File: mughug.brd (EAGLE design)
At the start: 68.2 x 17.8 mm, 9 parts, among them J1 NEOPIXEL, U1 DS18B20

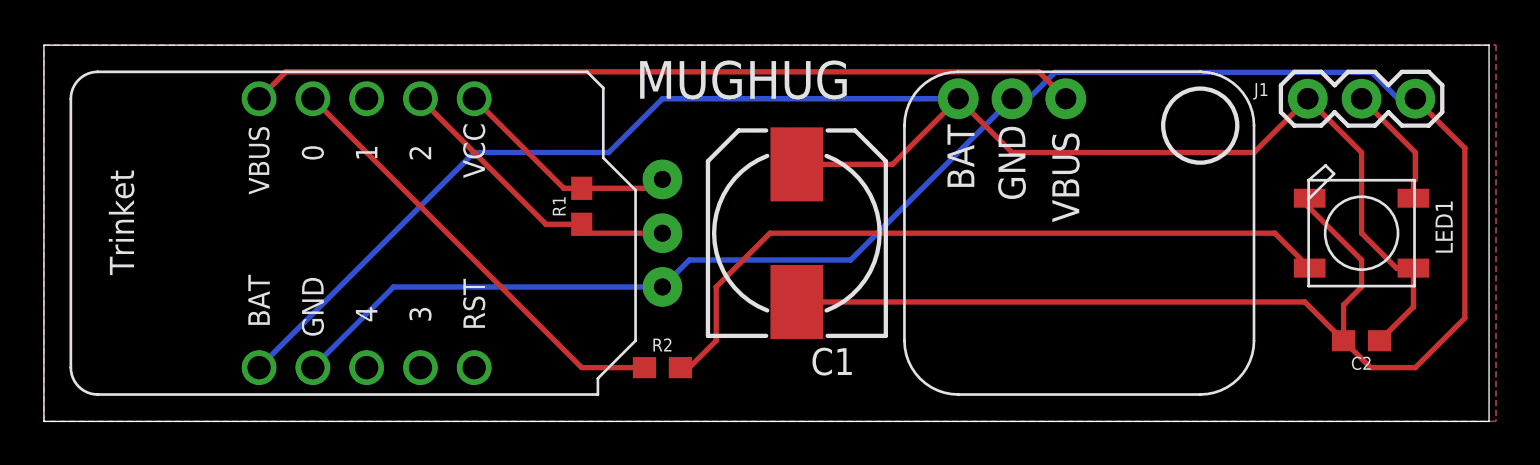
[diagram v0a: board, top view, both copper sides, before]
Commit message: Board reshuffle for oshpark
Added thicker board outline
moved neopixel to board center
small passived aligned same direction
12mil track for VBAT
added silkscreen
added corner holes for attachment
crossed fingers
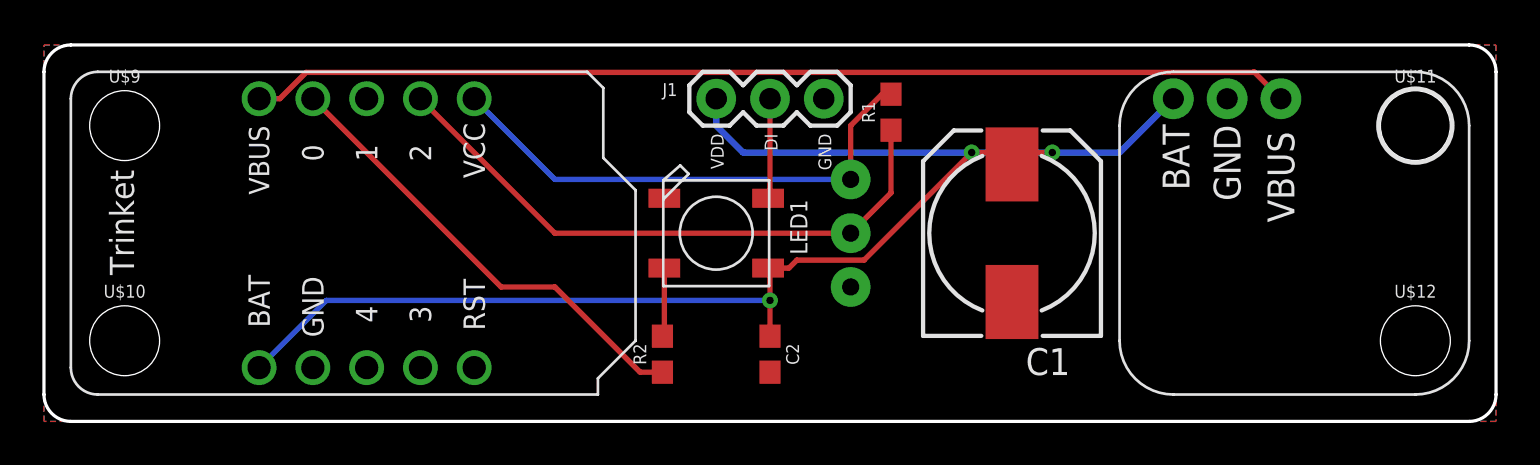
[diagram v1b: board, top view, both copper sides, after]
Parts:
- added U$10, U$11, U$12, U$9: (no value), SparkFun-Hardware:STAND-OFF
- moved LED1 30.5 mm to (31.8, 8.89)
- moved C2 27.9 mm to (34.3, 3.17), turned to 270 degrees
- moved J1 27.9 mm to (31.8, 15.2)
- moved R1 15.3 mm to (40.0, 14.6)
- moved U$2 10.2 mm to (58.4, 8.89)
- moved C1 10.2 mm to (45.7, 8.89)
- moved U1 8.89 mm to (38.1, 8.89)
- moved R2 0.63 mm to (29.2, 3.17), turned to 90 degrees
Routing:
- net GND: track 111.7 -> 0.00 mm
- net N$1: track 34.5 -> 3.25 mm
- net D2: track 14.1 -> 28.6 mm
- net VCC: track 10.8 -> 24.4 mm
- net VBAT: track 80.4 -> 69.2 mm, vias 0 -> 3
- net VBUS: track 39.2 -> 49.3 mm
- net N$4: track 5.79 -> 4.74 mm
- net D0: track 20.9 -> 21.9 mm
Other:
- board size 68.2 x 17.8 mm -> 68.6 x 17.8 mm
- board text added: "DI"
- board text added: "GND"
- board text added: "Troop 30226 TECHNOMANCERS"
- board text added: "VDD"

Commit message: Final tweak for oshpark proto order
oshpark order dm4ze97u
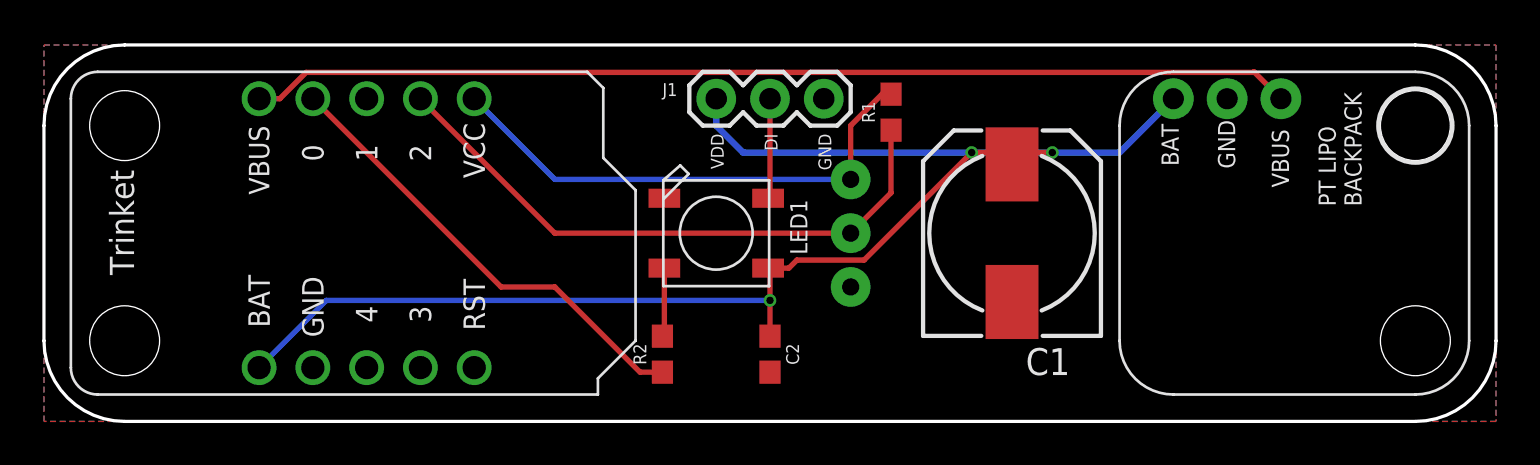
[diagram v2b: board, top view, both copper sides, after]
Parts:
- U$10, U$11, U$12, U$9: device SparkFun-Hardware:STAND-OFF -> redhunter:STAND-OFF
- U$2: value PROTRINKETLIPONOHOLE -> PROTRINKETLIPO
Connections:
- net VBUS: now also U$2.5V; no longer U$2.VBUS
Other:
- outline, holes or cut-outs redrawn
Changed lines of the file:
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@@
 <board>
 <plain>
-<wire x1="1.27" y1="0" x2="67.31" y2="0" width="0.1524" layer="20"/>
 <text x="54.61" y="3.81" size="1.778" layer="22" rot="MR0">MUGHUG</text>
-<wire x1="0" y1="16.51" x2="0" y2="1.27" width="0.1524" layer="20"/>
-<wire x1="1.27" y1="0" x2="0" y2="1.27" width="0.1524" layer="20" curve="-90"/>
-<wire x1="0" y1="16.51" x2="1.27" y2="17.78" width="0.1524" layer="20" curve="-90"/>
-<wire x1="67.31" y1="17.78" x2="68.58" y2="16.51" width="0.1524" layer="20" curve="-90"/>
-<wire x1="68.58" y1="16.51" x2="68.58" y2="1.27" width="0.1524" layer="20"/>
-<wire x1="1.27" y1="17.78" x2="67.31" y2="17.78" width="0.1524" layer="20"/>
-<wire x1="68.58" y1="1.27" x2="67.31" y2="0" width="0.1524" layer="20" curve="-90"/>
+<wire x1="3.81" y1="0" x2="64.77" y2="0" width="0.1524" layer="20"/>
+<wire x1="0" y1="13.97" x2="0" y2="3.81" width="0.1524" layer="20"/>
+<wire x1="68.58" y1="13.97" x2="68.58" y2="3.81" width="0.1524" layer="20"/>
+<wire x1="3.81" y1="17.78" x2="64.77" y2="17.78" width="0.1524" layer="20"/>
 <text x="31.496" y="13.589" size="0.6096" layer="21" font="vector" ratio="12" rot="R270">VDD</text>
 <text x="34.036" y="13.589" size="0.6096" layer="21" font="vector" ratio="12" rot="R270">DI</text>
@@
 <text x="33.02" y="5.08" size="2.54" layer="22" rot="MR0">Troop 30226
 TECHNOMANCERS</text>
+<wire x1="0" y1="13.97" x2="3.81" y2="17.78" width="0.1524" layer="20" curve="-90"/>
+<wire x1="64.77" y1="17.78" x2="68.58" y2="13.97" width="0.1524" layer="20" curve="-90"/>
+<wire x1="68.58" y1="3.81" x2="64.77" y2="0" width="0.1524" layer="20" curve="-90"/>
+<wire x1="3.81" y1="0" x2="0" y2="3.81" width="0.1524" layer="20" curve="-90"/>
 </plain>
 <attributes>
@@
 </class>
 </classes>
-<designrules name="default *">
-<description language="de">&lt;b&gt;EAGLE Design Rules&lt;/b&gt;
+<designrules name="oshpark-2layer-tented">
+<description language="en">&lt;b&gt;OSH Park Design Rules&lt;/b&gt;
 &lt;p&gt;
-Die Standard-Design-Rules sind so gewählt, dass sie für
-die meisten Anwendungen passen. Sollte ihre Platine
-besondere Anforderungen haben, treffen Sie die erforderlichen
-Einstellungen hier und speichern die Design Rules unter
-einem neuen Namen ab.</description>
-<description language="en">&lt;b&gt;EAGLE Design Rules&lt;/b&gt;
+Please make sure your boards conform to these design rules.
+&lt;/p&gt;
 &lt;p&gt;
-The default Design Rules have been set to cover
-a wide range of applications. Your particular design
-may have different requirements, so please make the
-necessary adjustments and save your customized
-design rules under a new name.</description>
+This DRC tents small vias, making them inaccessible on the produced board. This is great for dense routing, BGA, or production boards.
+&lt;/p&gt;
+&lt;p&gt;
+Note, that not all DRC settings must be set by the manufacturer. Several can be adjusted for the design, including those listed on our docs page here.
+&lt;a href=&quot;http://docs.oshpark.com/design-tools/eagle/design-rules-files/&quot;&gt;Adjustable Settings&lt;/a&gt;
+&lt;/p&gt;</description>
 <param name="layerSetup" value="(1*16)"/>
-<param name="mtCopper" value="0.035mm 0.035mm 0.035mm 0.035mm 0.035mm 0.035mm 0.035mm 0.035mm 0.035mm 0.035mm 0.035mm 0.035mm 0.035mm 0.035mm 0.035mm 0.035mm"/>
-<param name="mtIsolate" value="1.5mm 0.15mm 0.2mm 0.15mm 0.2mm 0.15mm 0.2mm 0.15mm 0.2mm 0.15mm 0.2mm 0.15mm 0.2mm 0.15mm 0.2mm"/>
+<param name="mtCopper" value="0.035559375mm 0.0356mm 0.0356mm 0.0356mm 0.0356mm 0.0356mm 0.0356mm 0.0356mm 0.0356mm 0.0356mm 0.0356mm 0.0356mm 0.0356mm 0.0356mm 0.0356mm 0.035559375mm"/>
+<param name="mtIsolate" value="1.6mm 0.1499mm 0.2007mm 0.1499mm 0.2007mm 0.1499mm 0.2007mm 0.1499mm 0.2007mm 0.1499mm 0.2007mm 0.1499mm 0.2007mm 0.1499mm 0.2007mm"/>
 <param name="mdWireWire" value="6mil"/>
 <param name="mdWirePad" value="6mil"/>
@@
 <param name="mdSmdVia" value="6mil"/>
 <param name="mdSmdSmd" value="6mil"/>
-<param name="mdViaViaSameLayer" value="6mil"/>
+<param name="mdViaViaSameLayer" value="8mil"/>
 <param name="mnLayersViaInSmd" value="2"/>
-<param name="mdCopperDimension" value="30mil"/>
+<param name="mdCopperDimension" value="15mil"/>
 <param name="mdDrill" value="6mil"/>
 <param name="mdSmdStop" value="0mil"/>
 <param name="msWidth" value="6mil"/>
-<param name="msDrill" value="0.35mm"/>
-<param name="msMicroVia" value="9.99mm"/>
+<param name="msDrill" value="10mil"/>
+<param name="msMicroVia" value="10mil"/>
 <param name="msBlindViaRatio" value="0.5"/>
 <param name="rvPadTop" value="0.25"/>
@@
 <param name="rvMicroViaOuter" value="0.25"/>
 <param name="rvMicroViaInner" value="0.25"/>
-<param name="rlMinPadTop" value="10mil"/>
+<param name="rlMinPadTop" value="5mil"/>
 <param name="rlMaxPadTop" value="20mil"/>
-<param name="rlMinPadInner" value="10mil"/>
+<param name="rlMinPadInner" value="5mil"/>
 <param name="rlMaxPadInner" value="20mil"/>
-<param name="rlMinPadBottom" value="10mil"/>
+<param name="rlMinPadBottom" value="5mil"/>
 <param name="rlMaxPadBottom" value="20mil"/>
-<param name="rlMinViaOuter" value="8mil"/>
+<param name="rlMinViaOuter" value="5mil"/>
 <param name="rlMaxViaOuter" value="20mil"/>
-<param name="rlMinViaInner" value="8mil"/>
+<param name="rlMinViaInner" value="5mil"/>
 <param name="rlMaxViaInner" value="20mil"/>
-<param name="rlMinMicroViaOuter" value="4mil"/>
+<param name="rlMinMicroViaOuter" value="5mil"/>
 <param name="rlMaxMicroViaOuter" value="20mil"/>
-<param name="rlMinMicroViaInner" value="4mil"/>
+<param name="rlMinMicroViaInner" value="5mil"/>
 <param name="rlMaxMicroViaInner" value="20mil"/>
 <param name="psTop" value="-1"/>
@@
 <param name="mvStopFrame" value="1"/>
 <param name="mvCreamFrame" value="0"/>
-<param name="mlMinStopFrame" value="4mil"/>
-<param name="mlMaxStopFrame" value="4mil"/>
+<param name="mlMinStopFrame" value="2.5mil"/>
+<param name="mlMaxStopFrame" value="2.5mil"/>
 <param name="mlMinCreamFrame" value="0mil"/>
 <param name="mlMaxCreamFrame" value="0mil"/>
-<param name="mlViaStopLimit" value="25mil"/>
+<param name="mlViaStopLimit" value="20mil"/>
 <param name="srRoundness" value="0"/>
 <param name="srMinRoundness" value="0mil"/>
@@
 </element>
 <element name="U$1" library="redhunter" package="TRINKET_NOHOLES" value="TRINKETNOHOLES" x="13.97" y="8.89" rot="R90"/>
-<element name="U$2" library="redhunter" package="PROTRINKETLIPO_NOHOLE" value="PROTRINKETLIPONOHOLE" x="58.42" y="8.89"/>
+<element name="U$2" library="redhunter" package="PROTRINKETLIPO_NOHOLE" value="PROTRINKETLIPO" x="58.42" y="8.89"/>
 <element name="U1" library="SparkFun-Sensors" package="TO-92-AMMO" value="DS18B20" x="38.1" y="8.89" rot="MR90">
 <attribute name="STORE_ID" value="SEN-00245" x="38.1" y="8.89" size="1.778" layer="28" rot="MR90" display="off"/>
@@
 <attribute name="PROD_ID" value="RES-07869" x="40.005" y="14.605" size="1.778" layer="27" rot="R90" display="off"/>
 </element>
-<element name="U$9" library="SparkFun-Hardware" package="STAND-OFF" value="" x="3.81" y="13.97"/>
-<element name="U$10" library="SparkFun-Hardware" package="STAND-OFF" value="" x="3.81" y="3.81"/>
-<element name="U$11" library="SparkFun-Hardware" package="STAND-OFF" value="" x="64.77" y="13.97"/>
-<element name="U$12" library="SparkFun-Hardware" package="STAND-OFF" value="" x="64.77" y="3.81"/>
+<element name="U$9" library="redhunter" package="STAND-OFF" value="" x="3.81" y="13.97"/>
+<element name="U$10" library="redhunter" package="STAND-OFF" value="" x="3.81" y="3.81"/>
+<element name="U$11" library="redhunter" package="STAND-OFF" value="" x="64.77" y="13.97"/>
+<element name="U$12" library="redhunter" package="STAND-OFF" value="" x="64.77" y="3.81"/>
 </elements>
 <signals>
@@
 <signal name="VBUS">
 <contactref element="U$1" pad="VBUS"/>
-<contactref element="U$2" pad="VBUS"/>
+<contactref element="U$2" pad="5V"/>
 <wire x1="10.16" y1="15.24" x2="11.1381375" y2="15.24" width="0.254" layer="1"/>
 <wire x1="57.1246" y1="16.4846" x2="57.15" y2="16.51" width="0.254" layer="1"/>
